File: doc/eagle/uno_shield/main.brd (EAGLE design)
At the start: 58.7 x 58.4 mm, 15 parts, among them U1 ARDUINOR3-BPLACE

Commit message: [ add ] routed board, main.png
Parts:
- removed R2, R4: 1k, rcl:0204/5
- removed R3: (no value), rcl:RTRIM64X
- added R8: (no value), resistor:RTRIM3339P
- R1: device rcl:RTRIM64X -> resistor:RTRIM3339P
- moved R7 29.6 mm to (26.0, 31.8), flipped to the bottom
- moved S3 21.0 mm to (30.5, 22.9), flipped to the bottom, turned to 180 degrees
- moved S1 11.4 mm to (49.5, 27.9), flipped to the bottom, turned to 270 degrees
- moved S2 9.61 mm to (40.0, 22.9), flipped to the bottom, turned to 180 degrees
- moved S4 8.89 mm to (49.5, 17.8), flipped to the bottom, turned to 90 degrees
- moved U1 2.84 mm to (-14.0, 1.27)
- moved JP1 2.62 mm to (38.7, 40.6), flipped to the bottom
- moved R1 2.29 mm to (17.8, 22.9), flipped to the bottom, turned to 0 degrees
- moved LED2 2.29 mm to (9.53, 31.8), flipped to the bottom
- moved R6 2.01 mm to (9.53, 41.3)
- moved LED1 1.80 mm to (17.8, 31.8), flipped to the bottom
- moved R5 1.42 mm to (17.8, 41.3)
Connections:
- removed net N$1: R1.3, R2.1
- removed net N$2: R3.3, R4.1
- net ADC_VCAP: now also R8.2; no longer R1.2
- net ADC_VOUT: now also R1.2; no longer R3.2
- net BUT_MINUS: now also S4.1, S4.2, U1.A5; no longer S2.1, S2.2, U1.A3
- net BUT_MODE: now also S2.1, S2.2, U1.A3; no longer S1.1, S1.2, U1.A4
- net BUT_PLUS: now also S1.1, S1.2, U1.A4; no longer S3.1, S3.2, U1.A2
- net BUT_SAVE: now also S3.1, S3.2, U1.A2; no longer S4.1, S4.2, U1.A5
- net GND: now also R1.3, R8.3; no longer R2.2, R4.2
- net LCD_EN: now also U1.D6; no longer U1.D7
- net LCD_RS: now also U1.D7; no longer U1.D6
- net UNO_5V: now also R8.1; no longer R3.1
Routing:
- net LCD_RS: track 44.5 -> 14.5 mm, vias 0 -> 1
- net BUT_SAVE: track 6.50 -> 30.4 mm, vias 0 -> 1
- net BUT_MINUS: track 34.0 -> 18.1 mm, vias 0 -> 1
- net BUT_PLUS: track 44.6 -> 29.5 mm, vias 0 -> 1
- net LCD_DB7: track 16.5 -> 31.5 mm, vias 0 -> 1
- net LCD_EN: track 29.2 -> 14.5 mm, vias 0 -> 1
- net UNO_5V: track 100.3 -> 86.5 mm
- net LCD_DB6: track 11.4 -> 22.0 mm, vias 0 -> 1
- net ADC_VOUT: track 26.7 -> 35.9 mm, vias 0 -> 1
- net GND: track 0.00 -> 6.98 mm, vias 0 -> 1
- net ADC_VCAP: track 36.2 -> 41.8 mm, vias 0 -> 1
- net LCD_VO: track 14.0 -> 17.9 mm
- net BUT_MODE: track 20.0 -> 23.8 mm, vias 0 -> 1
- net LCD_DB4: track 14.0 -> 10.4 mm, vias 0 -> 1
- net N$2: track 3.18 -> 0.00 mm
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- added copper zone on layer 16, net GND
- removed copper zone on layer 1, net GND
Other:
- board size 58.7 x 58.4 mm -> 55.5 x 56.5 mm

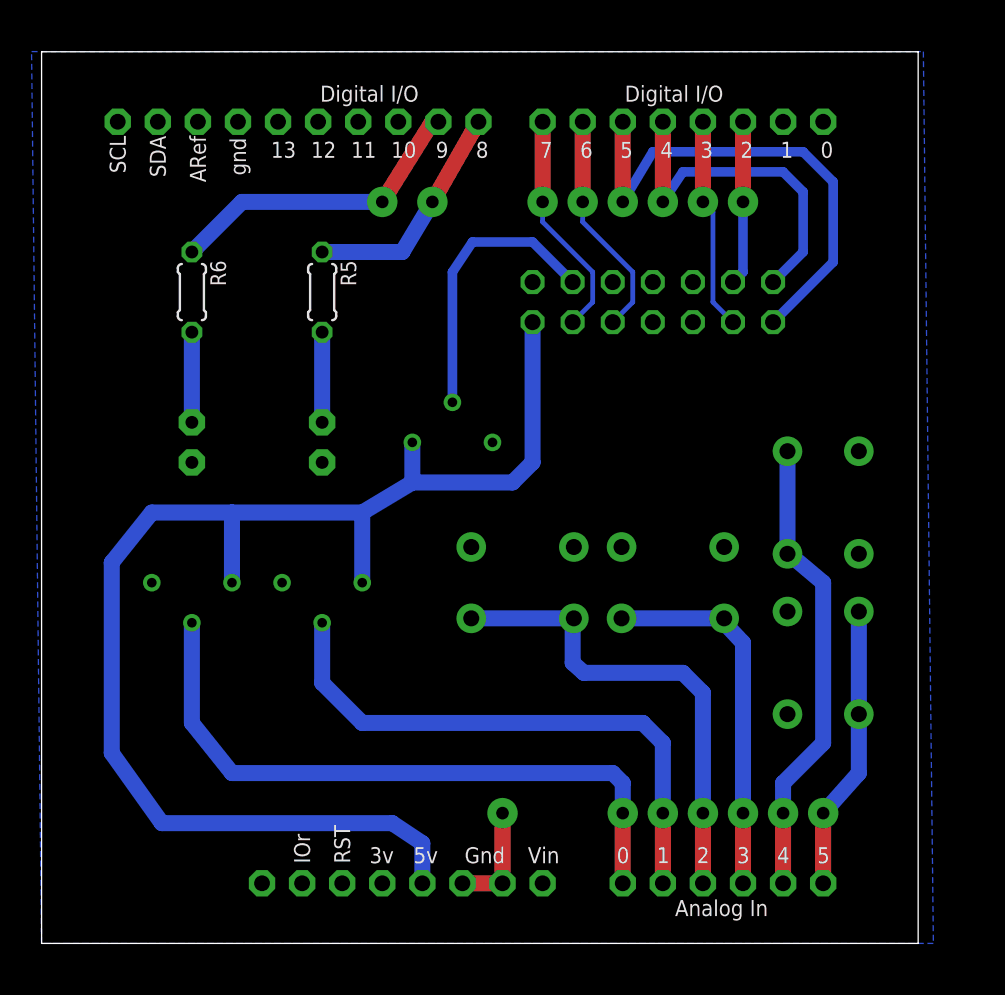
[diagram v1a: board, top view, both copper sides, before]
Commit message: [ fix ] uno_shield board
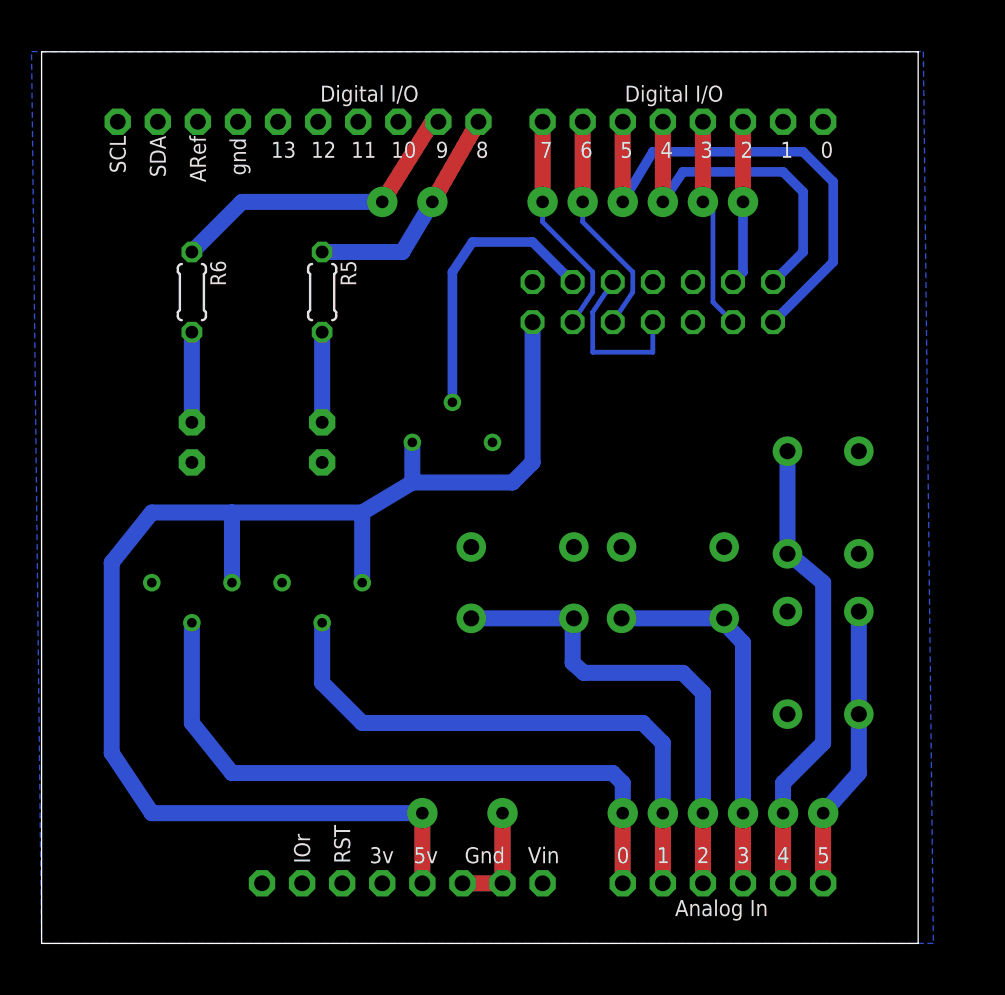
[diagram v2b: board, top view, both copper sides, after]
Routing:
- net GND: track 6.98 -> 17.5 mm
- net UNO_5V: track 86.5 -> 87.8 mm, vias 0 -> 1
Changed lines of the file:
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@@
 <grid distance="0.635" unitdist="mm" unit="mm" style="lines" multiple="1" display="yes" altdistance="0.025" altunitdist="inch" altunit="inch"/>
 <layers>
-<layer number="1" name="Top" color="4" fill="1" visible="no" active="yes"/>
+<layer number="1" name="Top" color="4" fill="1" visible="yes" active="yes"/>
 <layer number="16" name="Bottom" color="1" fill="1" visible="yes" active="yes"/>
 <layer number="17" name="Pads" color="2" fill="1" visible="yes" active="yes"/>
 <layer number="18" name="Vias" color="2" fill="1" visible="yes" active="yes"/>
-<layer number="19" name="Unrouted" color="6" fill="1" visible="no" active="yes"/>
+<layer number="19" name="Unrouted" color="6" fill="1" visible="yes" active="yes"/>
 <layer number="20" name="Dimension" color="15" fill="1" visible="yes" active="yes"/>
-<layer number="21" name="tPlace" color="7" fill="1" visible="no" active="yes"/>
-<layer number="22" name="bPlace" color="7" fill="1" visible="no" active="yes"/>
-<layer number="23" name="tOrigins" color="15" fill="1" visible="no" active="yes"/>
-<layer number="24" name="bOrigins" color="15" fill="1" visible="no" active="yes"/>
-<layer number="25" name="tNames" color="7" fill="1" visible="no" active="yes"/>
+<layer number="21" name="tPlace" color="7" fill="1" visible="yes" active="yes"/>
+<layer number="22" name="bPlace" color="7" fill="1" visible="yes" active="yes"/>
+<layer number="23" name="tOrigins" color="15" fill="1" visible="yes" active="yes"/>
+<layer number="24" name="bOrigins" color="15" fill="1" visible="yes" active="yes"/>
+<layer number="25" name="tNames" color="7" fill="1" visible="yes" active="yes"/>
 <layer number="26" name="bNames" color="7" fill="1" visible="no" active="yes"/>
 <layer number="27" name="tValues" color="7" fill="1" visible="no" active="yes"/>
@@
 <vertex x="0" y="0"/>
 </polygon>
-<wire x1="38.735" y1="41.91" x2="36.195" y2="41.91" width="0" layer="19" extent="1-1"/>
+<wire x1="36.195" y1="41.91" x2="34.925" y2="40.005" width="0.3048" layer="16"/>
+<wire x1="34.925" y1="40.005" x2="34.925" y2="37.465" width="0.3048" layer="16"/>
+<wire x1="38.735" y1="39.37" x2="38.735" y2="37.465" width="0.3048" layer="16"/>
+<wire x1="38.735" y1="37.465" x2="34.925" y2="37.465" width="0.3048" layer="16"/>
 </signal>
 <signal name="VIN">
@@
 <contactref element="R1" pad="1"/>
 <contactref element="R8" pad="1"/>
-<wire x1="24.13" y1="3.81" x2="24.13" y2="6.35" width="1.016" layer="16"/>
-<wire x1="24.13" y1="6.35" x2="22.225" y2="7.62" width="1.016" layer="16"/>
-<wire x1="22.225" y1="7.62" x2="7.62" y2="7.62" width="1.016" layer="16"/>
-<wire x1="7.62" y1="7.62" x2="4.445" y2="12.065" width="1.016" layer="16"/>
-<wire x1="4.445" y1="12.065" x2="4.445" y2="24.13" width="1.016" layer="16"/>
 <wire x1="4.445" y1="24.13" x2="6.985" y2="27.305" width="1.016" layer="16"/>
 <wire x1="23.495" y1="31.75" x2="23.495" y2="29.21" width="1.016" layer="16"/>
@@
 <wire x1="12.065" y1="22.86" x2="12.065" y2="27.305" width="1.016" layer="16"/>
 <wire x1="20.32" y1="22.86" x2="20.32" y2="27.305" width="1.016" layer="16"/>
+<wire x1="24.13" y1="3.81" x2="24.13" y2="8.255" width="1.016" layer="1"/>
+<via x="24.13" y="8.255" extent="1-16" drill="0.8" diameter="1.9304"/>
+<wire x1="4.445" y1="24.13" x2="4.445" y2="12.065" width="1.016" layer="16"/>
+<wire x1="4.445" y1="12.065" x2="6.985" y2="8.255" width="1.016" layer="16"/>
+<wire x1="6.985" y1="8.255" x2="24.13" y2="8.255" width="1.016" layer="16"/>
 </signal>
 <signal name="N$3">
@@
 <wire x1="31.75" y1="46.99" x2="31.75" y2="45.72" width="0.3048" layer="16"/>
 <wire x1="31.75" y1="45.72" x2="34.925" y2="42.545" width="0.3048" layer="16"/>
-<wire x1="34.925" y1="42.545" x2="34.925" y2="40.64" width="0.3048" layer="16"/>
-<wire x1="34.925" y1="40.64" x2="33.655" y2="39.37" width="0.3048" layer="16"/>
+<wire x1="34.925" y1="42.545" x2="34.925" y2="41.275" width="0.3048" layer="16"/>
+<wire x1="34.925" y1="41.275" x2="33.655" y2="39.37" width="0.3048" layer="16"/>
 </signal>
 <signal name="LCD_EN">
@@
 <wire x1="34.29" y1="46.99" x2="34.29" y2="45.72" width="0.3048" layer="16"/>
 <wire x1="34.29" y1="45.72" x2="37.465" y2="42.545" width="0.3048" layer="16"/>
-<wire x1="37.465" y1="42.545" x2="37.465" y2="40.64" width="0.3048" layer="16"/>
-<wire x1="37.465" y1="40.64" x2="36.195" y2="39.37" width="0.3048" layer="16"/>
+<wire x1="37.465" y1="42.545" x2="37.465" y2="41.275" width="0.3048" layer="16"/>
+<wire x1="37.465" y1="41.275" x2="36.195" y2="39.37" width="0.3048" layer="16"/>
 </signal>
 <signal name="LCD_DB4">
